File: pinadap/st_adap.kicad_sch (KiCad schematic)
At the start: 5 parts, among them J1 Conn_02x07_Odd_Even, J2 Conn_01x05_Socket, J3 Conn_01x05_Socket, J4 Conn_01x05_Socket, J5 Conn_01x03_Socket

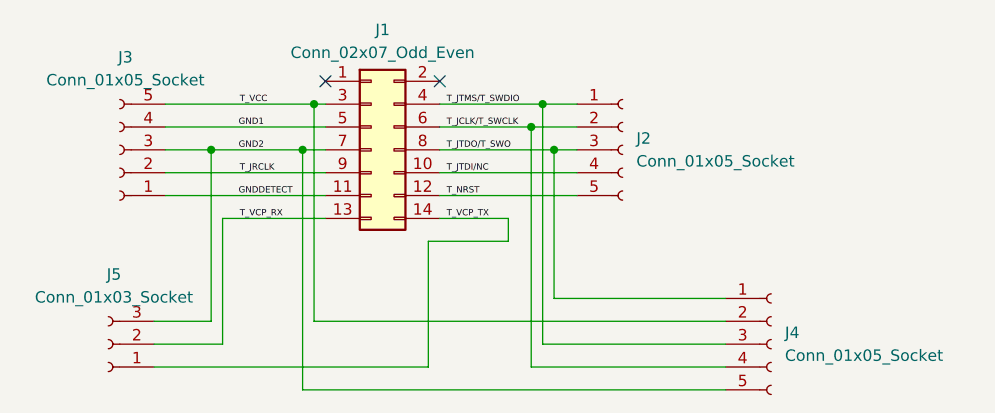
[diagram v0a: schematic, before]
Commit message: 1.27mm connector with key
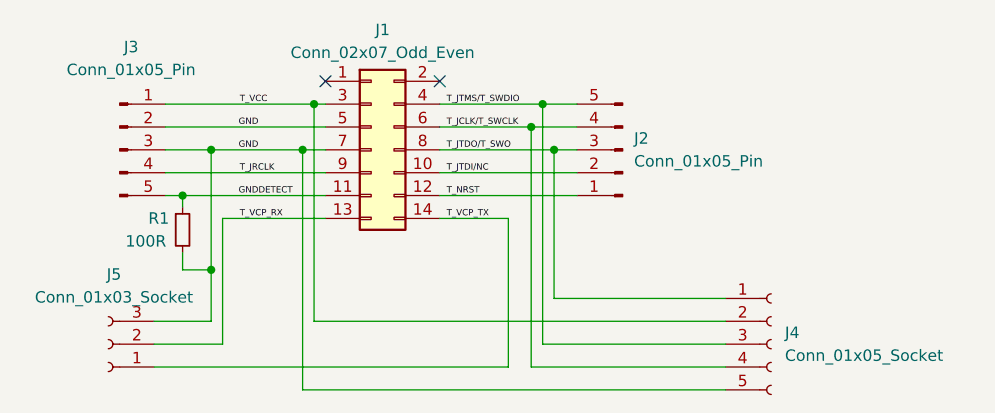
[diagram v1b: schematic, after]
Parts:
- removed J2, J3: Conn_01x05_Socket, Connector_PinHeader_2.54mm:PinHeader_1x05_P2.54mm_Vertical, symbol Connector:Conn_01x05_Socket
- added J2, J3: Conn_01x05_Pin, Connector_PinHeader_2.54mm:PinHeader_1x05_P2.54mm_Vertical, symbol Connector:Conn_01x05_Pin
- added R1: 100R, Resistor_SMD:R_0805_2012Metric_Pad1.20x1.40mm_HandSolder, symbol Device:R_Small
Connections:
- net GND2 is gone; now on net GND: J1.7 (Pin_7), J4.5 (Pin_5), J5.3 (Pin_3)
- net GNDDETECT: now also J3.5 (Pin_5), R1.1
- net T_JCLK/T_SWCLK: now also J2.4 (Pin_4)
- net T_JRCLK: now also J3.4 (Pin_4)
- net T_JTDI/NC: now also J2.2 (Pin_2)
- net T_JTDO/T_SWO: now also J2.3 (Pin_3)
- net T_JTMS/T_SWDIO: now also J2.5 (Pin_5)
- net T_NRST: now also J2.1 (Pin_1)
- net T_VCC: now also J3.1 (Pin_1)
- net GND1 renamed GND
- net GND: now also J3.2 (Pin_2), J3.3 (Pin_3), R1.2
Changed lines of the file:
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@@
   (junction (at 118.11 45.72) (diameter 0) (color 0 0 0 0)
   )
+  (junction (at 79.375 53.34) (diameter 0) (color 0 0 0 0)
+  )
   (junction (at 120.65 48.26) (diameter 0) (color 0 0 0 0)
+  )
+  (junction (at 82.55 61.595) (diameter 0) (color 0 0 0 0)
   )
   (junction (at 82.55 48.26) (diameter 0) (color 0 0 0 0)
@@
   (no_connect (at 95.25 40.64))
   (no_connect (at 107.95 40.64))
+  (wire (pts (xy 82.55 61.595) (xy 82.55 67.31))
+    (stroke (width 0) (type default))
+  )
   (wire (pts (xy 93.98 43.18) (xy 93.98 67.31))
     (stroke (width 0) (type default))
   )
-  (wire (pts (xy 77.47 53.34) (xy 95.25 53.34))
-    (stroke (width 0) (type default))
-  )
-  (wire (pts (xy 76.2 72.39) (xy 106.68 72.39))
+  (wire (pts (xy 77.47 53.34) (xy 79.375 53.34))
+    (stroke (width 0) (type default))
+  )
+  (wire (pts (xy 76.2 72.39) (xy 115.57 72.39))
     (stroke (width 0) (type default))
   )
@@
     (stroke (width 0) (type default))
   )
+  (wire (pts (xy 79.375 53.34) (xy 95.25 53.34))
+    (stroke (width 0) (type default))
+  )
   (wire (pts (xy 107.95 50.8) (xy 123.19 50.8))
     (stroke (width 0) (type default))
@@
     (stroke (width 0) (type default))
   )
-  (wire (pts (xy 82.55 48.26) (xy 82.55 67.31))
+  (wire (pts (xy 82.55 48.26) (xy 82.55 61.595))
     (stroke (width 0) (type default))
   )
@@
     (stroke (width 0) (type default))
   )
+  (wire (pts (xy 79.375 53.34) (xy 79.375 54.61))
+    (stroke (width 0) (type default))
+  )
   (wire (pts (xy 92.71 48.26) (xy 92.71 74.93))
     (stroke (width 0) (type default))
@@
     (stroke (width 0) (type default))
   )
+  (wire (pts (xy 79.375 59.69) (xy 79.375 61.595))
+    (stroke (width 0) (type default))
+  )
   (wire (pts (xy 92.71 74.93) (xy 139.7 74.93))
     (stroke (width 0) (type default))
@@
     (stroke (width 0) (type default))
   )
-  (wire (pts (xy 106.68 58.42) (xy 115.57 58.42))
+  (wire (pts (xy 79.375 61.595) (xy 82.55 61.595))
     (stroke (width 0) (type default))
   )
@@
     (stroke (width 0) (type default))
   )
-  (wire (pts (xy 115.57 58.42) (xy 115.57 55.88))
-    (stroke (width 0) (type default))
-  )
   (wire (pts (xy 93.98 43.18) (xy 95.25 43.18))
     (stroke (width 0) (type default))
   )
-  (wire (pts (xy 106.68 72.39) (xy 106.68 58.42))
+  (wire (pts (xy 115.57 55.88) (xy 115.57 72.39))
     (stroke (width 0) (type default))
   )
@@
     (effects (font (size 0.7 0.7)) (justify left bottom))
   )
-  (label "GND2" (at 85.598 48.26 0) (fields_autoplaced)
+  (label "GND" (at 85.598 48.26 0) (fields_autoplaced)
     (effects (font (size 0.7 0.7)) (justify left bottom))
   )
@@
     (effects (font (size 0.7 0.7)) (justify left bottom))
   )
-  (label "GND1" (at 85.598 45.72 0) (fields_autoplaced)
+  (label "GND" (at 85.598 45.72 0) (fields_autoplaced)
     (effects (font (size 0.7 0.7)) (justify left bottom))
   )
@@
     )
   )
-  (symbol (lib_id "Connector:Conn_01x05_Socket") (at 72.39 48.26 180) (unit 1)
-    (in_bom yes) (on_board yes) (dnp no) (fields_autoplaced)
-    (property "Reference" "J3" (at 73.025 37.973 0)
-      (effects (font (size 1.27 1.27)))
-    )
-    (property "Value" "Conn_01x05_Socket" (at 73.025 40.513 0)
-      (effects (font (size 1.27 1.27)))
-    )
-    (property "Footprint" "Connector_PinHeader_2.54mm:PinHeader_1x05_P2.54mm_Vertical" (at 72.39 48.26 0)
-      (effects (font (size 1.27 1.27)) hide)
-    )
-    (property "Datasheet" "~" (at 72.39 48.26 0)
-      (effects (font (size 1.27 1.27)) hide)
-    )
-    (property "JLC#" "" (at 72.39 48.26 0)
-      (effects (font (size 1.27 1.27)) hide)
-    )
-    (pin "1")
-    (pin "2")
-    (pin "3")
-    (pin "4")
-    (pin "5")
-    (instances
-      (project "st_adap"
-        (path "/6c75ccde-3fe8-449f-9ae7-ddec10254c91"
-          (reference "J3") (unit 1)
-        )
-      )
-    )
-  )
-  (symbol (lib_id "Connector:Conn_01x05_Socket") (at 128.27 48.26 0) (unit 1)
-    (in_bom yes) (on_board yes) (dnp no) (fields_autoplaced)
-    (property "Reference" "J2" (at 129.794 46.99 0)
-      (effects (font (size 1.27 1.27)) (justify left))
-    )
-    (property "Value" "Conn_01x05_Socket" (at 129.794 49.53 0)
-      (effects (font (size 1.27 1.27)) (justify left))
-    )
-    (property "Footprint" "Connector_PinHeader_2.54mm:PinHeader_1x05_P2.54mm_Vertical" (at 128.27 48.26 0)
-      (effects (font (size 1.27 1.27)) hide)
-    )
-    (property "Datasheet" "~" (at 128.27 48.26 0)
-      (effects (font (size 1.27 1.27)) hide)
-    )
-    (property "JLC#" "" (at 128.27 48.26 0)
-      (effects (font (size 1.27 1.27)) hide)
-    )
-    (pin "1")
-    (pin "2")
-    (pin "3")
-    (pin "4")
-    (pin "5")
-    (instances
-      (project "st_adap"
-        (path "/6c75ccde-3fe8-449f-9ae7-ddec10254c91"
-          (reference "J2") (unit 1)
-        )
-      )
-    )
-  )
   (symbol (lib_id "Connector_Generic:Conn_02x07_Odd_Even") (at 100.33 48.26 0) (unit 1)
     (in_bom yes) (on_board yes) (dnp no) (fields_autoplaced)
@@
       (effects (font (size 1.27 1.27)) hide)
     )
-    (property "Datasheet" "~" (at 100.33 48.26 0)
+    (property "Datasheet" "https://www.digikey.se/en/products/detail/samtec-inc/FTSH-107-01-L-DV-K/6678186" (at 100.33 48.26 0)
       (effects (font (size 1.27 1.27)) hide)
     )
@@
         )
       )
+    )
+  )
+  (symbol (lib_id "Connector:Conn_01x05_Pin") (at 128.27 48.26 180) (unit 1)
+    (in_bom yes) (on_board yes) (dnp no) (fields_autoplaced)
+    (property "Reference" "J2" (at 129.54 46.99 0)
+      (effects (font (size 1.27 1.27)) (justify right))
+    )
+    (property "Value" "Conn_01x05_Pin" (at 129.54 49.53 0)
+      (effects (font (size 1.27 1.27)) (justify right))
+    )
+    (property "Footprint" "Connector_PinHeader_2.54mm:PinHeader_1x05_P2.54mm_Vertical" (at 128.27 48.26 0)
+      (effects (font (size 1.27 1.27)) hide)
+    )
+    (property "Datasheet" "~" (at 128.27 48.26 0)
+      (effects (font (size 1.27 1.27)) hide)
+    )
+    (pin "4")
+    (pin "5")
+    (pin "3")
+    (pin "1")
+    (pin "2")
+    (instances
+      (project "st_adap"
+        (path "/6c75ccde-3fe8-449f-9ae7-ddec10254c91"
+          (reference "J2") (unit 1)
+        )
+      )
+    )
+  )
+  (symbol (lib_id "Device:R_Small") (at 79.375 57.15 0) (unit 1)
+    (in_bom yes) (on_board yes) (dnp no)
+    (property "Reference" "R1" (at 75.565 55.88 0)
+      (effects (font (size 1.27 1.27)) (justify left))
+    )
+    (property "Value" "100R" (at 73.025 58.42 0)
+      (effects (font (size 1.27 1.27)) (justify left))
+    )
+    (property "Footprint" "Resistor_SMD:R_0805_2012Metric_Pad1.20x1.40mm_HandSolder" (at 79.375 57.15 0)
+      (effects (font (size 1.27 1.27)) hide)
+    )
+    (property "Datasheet" "~" (at 79.375 57.15 0)
+      (effects (font (size 1.27 1.27)) hide)
+    )
+    (pin "1")
+    (pin "2")
+    (instances
+      (project "st_adap"
+        (path "/6c75ccde-3fe8-449f-9ae7-ddec10254c91"
+          (reference "R1") (unit 1)
+        )
+      )
+    )
+  )
+  (symbol (lib_id "Connector:Conn_01x05_Pin") (at 72.39 48.26 0) (unit 1)
+    (in_bom yes) (on_board yes) (dnp no)
+    (property "Reference" "J3" (at 73.66 36.83 0)
+      (effects (font (size 1.27 1.27)))
+    )
+    (property "Value" "Conn_01x05_Pin" (at 73.66 39.37 0)
+      (effects (font (size 1.27 1.27)))
+    )
+    (property "Footprint" "Connector_PinHeader_2.54mm:PinHeader_1x05_P2.54mm_Vertical" (at 72.39 48.26 0)
+      (effects (font (size 1.27 1.27)) hide)
+    )
+    (property "Datasheet" "~" (at 72.39 48.26 0)
+      (effects (font (size 1.27 1.27)) hide)
+    )
+    (pin "4")
+    (pin "5")
+    (pin "3")
+    (pin "1")
+    (pin "2")
+    (instances
+      (project "st_adap"
+        (path "/6c75ccde-3fe8-449f-9ae7-ddec10254c91"
+          (reference "J3") (unit 1)
+        )
+      )

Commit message: Generate fabrication files
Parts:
- J1: JLC# C2881912 -> (none)
- R1: JLC# (none) -> C17408
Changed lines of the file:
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@@
       (effects (font (size 1.27 1.27)) hide)
     )
-    (property "JLC#" "C2881912" (at 100.33 48.26 0)
+    (property "JLC#" "" (at 100.33 48.26 0)
       (effects (font (size 1.27 1.27)) hide)
     )
@@
       (effects (font (size 1.27 1.27)) hide)
     )
+    (property "JLC#" "C17408" (at 79.375 57.15 0)
+      (effects (font (size 1.27 1.27)) hide)
+    )
